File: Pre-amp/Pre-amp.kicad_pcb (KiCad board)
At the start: 2 copper layers, 182.9 x 53.3 mm, 137 parts, among them J1 In, J2 PWR, J3 Send, J4 Return, J5 Out, Q1 J113 NJFET, Q2 J113 NJFET, Q3 J113 NJFET, Q4 J113 NJFET, SW1 Jack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

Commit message: tweak PCB layout
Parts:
- C11, C12: value 0.01uf -> .01uf
- C13, C14: value 0.047uf -> .047uf
- C27: value 0.0047uf -> .0047uf
- C28: value 0.22uf -> .22uf
- C5: value 0.0033uf -> .0033uf
- C9: value 0.0022uf -> .0022uf
- D10: footprint LEDs:LED_D3.0mm -> Connector_PinHeader_2.00mm:PinHeader_2x01_P2.00mm_Vertical
- Q1, Q3: value J113 NJFET -> J113
- moved D10 20.0 mm to (125.5, 100.1), turned to 180 degrees
- moved R44 18.0 mm to (94.5, 64.3), turned to 90 degrees
- moved C19 13.2 mm to (130.1, 96.0), turned to 0 degrees
- moved R59 7.78 mm to (136.9, 98.0), turned to 0 degrees
- moved C17 7.34 mm to (89.2, 62.7)
- moved R46 5.66 mm to (98.6, 64.3), turned to 90 degrees
- moved R60 4.51 mm to (152.9, 83.8), turned to 0 degrees
- moved C29 4.15 mm to (145.1, 98.0)
- moved C33 4.02 mm to (109.0, 95.8)
- moved C18 3.82 mm to (127.0, 93.0), turned to 90 degrees
- moved R56 3.34 mm to (152.7, 79.2)
- moved C21 2.54 mm to (113.3, 73.7)
- moved C7 2.44 mm to (155.2, 60.5), turned to 180 degrees
- moved R61 2.30 mm to (157.7, 93.0)
- moved SW2 2.03 mm to (114.0, 100.1)
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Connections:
- J3 pad 3: (no net) -> Net-(J3-Pad3)
- J5 pad 3: (no net) -> Net-(J5-Pad3)
- SW1 pad 3: (no net) -> Net-(SW1-Pad3)
- SW2 pad 3: (no net) -> Net-(SW2-Pad3)
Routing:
- net F: track 80.1 -> 69.6 mm
- net D: track 55.6 -> 64.8 mm
- net B: track 11.8 -> 3.09 mm
- net DIST-IN: track 24.4 -> 32.8 mm
- net Net-(D10-Pad2): track 3.77 -> 7.39 mm
- net -15V: track 188.2 -> 184.7 mm
- net Net-(C26-Pad2): track 20.6 -> 17.3 mm
- net Net-(C21-Pad2): track 53.3 -> 51.0 mm
- net Net-(C6-Pad1): track 4.23 -> 6.49 mm
- net Net-(C8-Pad2): track 35.1 -> 36.8 mm
- net C: track 9.80 -> 11.4 mm
- net Net-(C8-Pad1): track 8.86 -> 10.4 mm
- net Net-(C20-Pad1): track 44.6 -> 46.0 mm
- net Net-(R13-Pad1): track 26.6 -> 27.6 mm
- net Net-(C33-Pad1): track 54.7 -> 55.7 mm
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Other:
- board text added: "MXM Designs Pre-Amp v1.2.0 05–11-2019"
- board text removed: "MXM Designs Pre-Amp v1.2.0 05–09-2019"

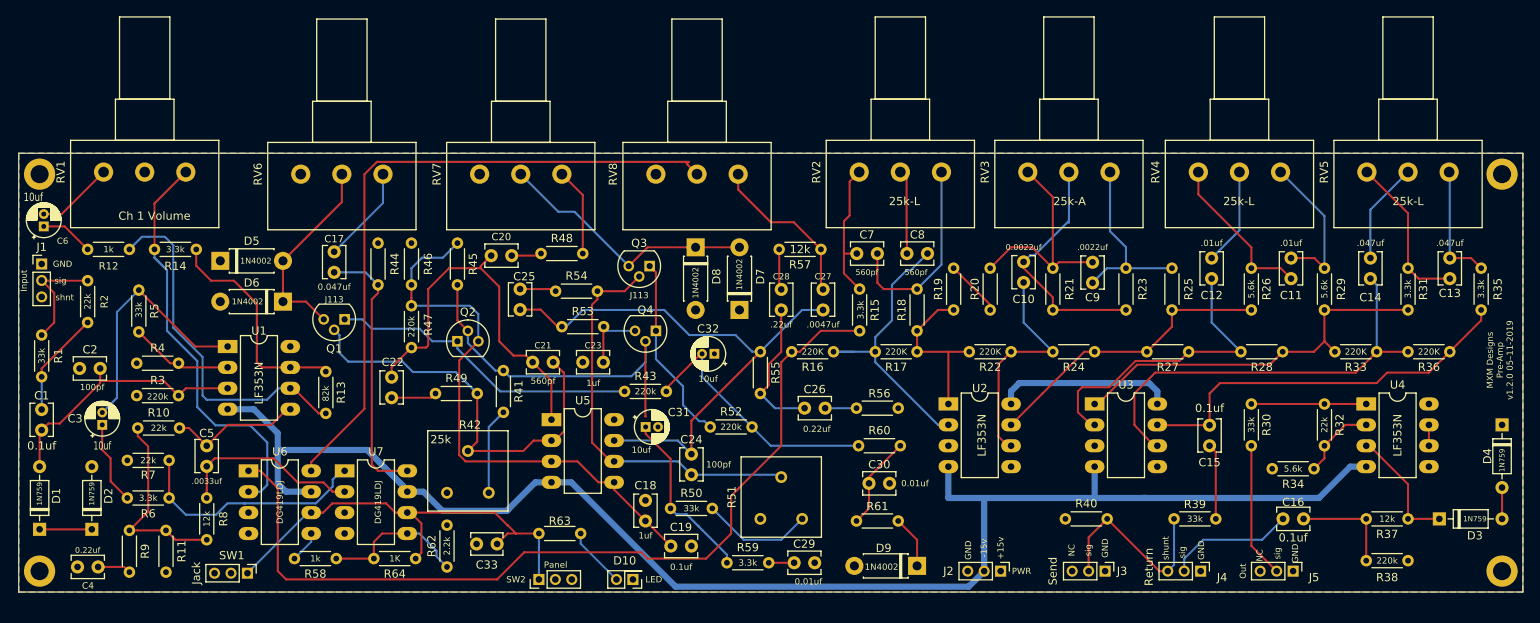
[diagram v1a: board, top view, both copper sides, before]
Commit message: add power caps
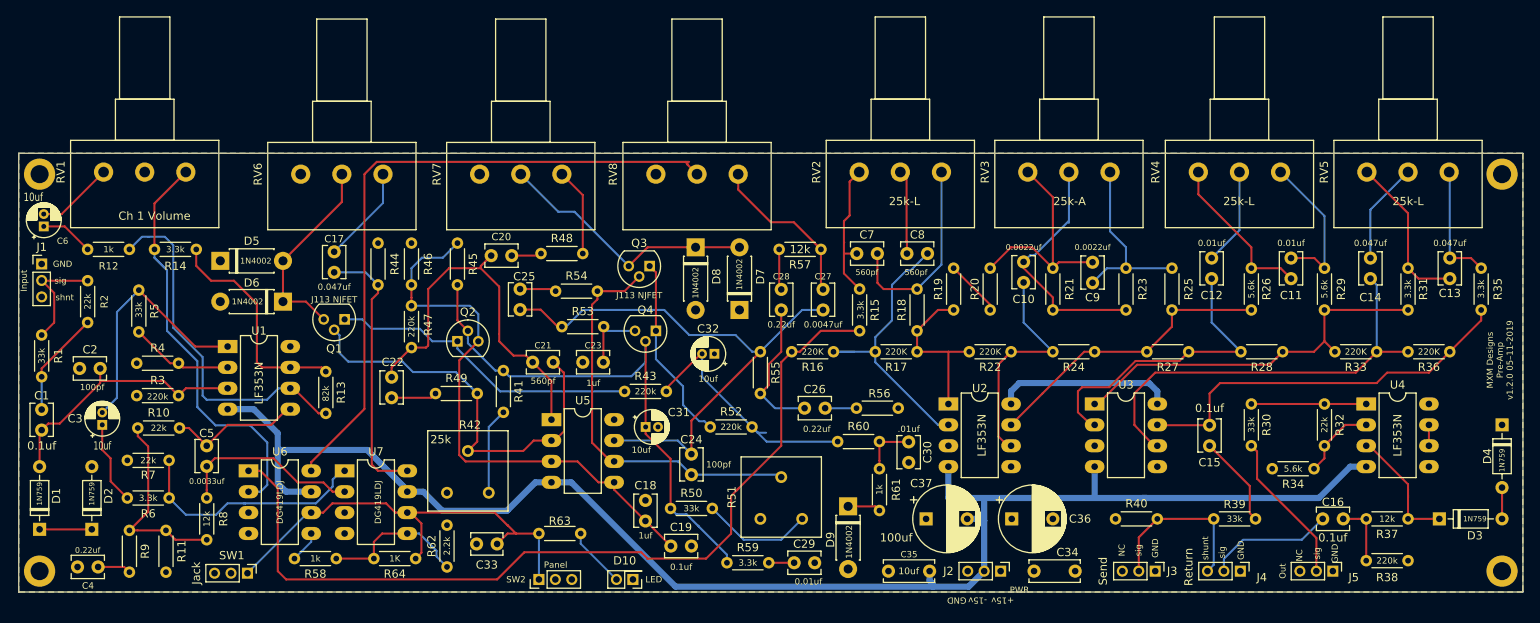
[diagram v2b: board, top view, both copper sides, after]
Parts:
- added C34: 10uf, Capacitor_THT:C_Disc_D6.0mm_W2.5mm_P5.00mm, F.Cu at (174.2, 99.1)
- added C35: 10uf, Capacitor_THT:C_Disc_D6.0mm_W2.5mm_P5.00mm, F.Cu at (156.5, 99.1)
- added C36: 100uf, Capacitor_THT:CP_Radial_D8.0mm_P5.00mm, F.Cu at (171.5, 92.7)
- added C37: 100uf, Capacitor_THT:CP_Radial_D8.0mm_P5.00mm, F.Cu at (161.1, 92.7)
- C11, C12: value .01uf -> 0.01uf
- C13, C14: value .047uf -> 0.047uf
- C27: value .0047uf -> 0.0047uf
- C28: value .22uf -> 0.22uf
- C30: value 0.01uf -> .01uf
- C5: value .0033uf -> 0.0033uf
- C9: value .0022uf -> 0.0022uf
- Q1, Q3: value J113 -> J113 NJFET
- moved D9 11.1 mm to (151.6, 91.2), turned to 270 degrees
- moved J3 6.10 mm to (189.0, 99.1)
- moved R40 6.10 mm to (184.2, 92.7)
- moved C16 4.83 mm to (209.3, 92.7)
- moved J4 4.83 mm to (199.3, 99.1)
- moved J5 4.83 mm to (210.6, 99.1)
- moved R39 4.83 mm to (196.1, 92.7)
- moved C30 3.44 mm to (159.0, 85.9), turned to 90 degrees
- moved R61 2.62 mm to (155.4, 91.7), turned to 90 degrees
- moved R60 2.59 mm to (150.4, 83.3)
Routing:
- net Net-(C16-Pad2): track 12.7 -> 7.87 mm
- net C: track 11.4 -> 6.87 mm
- net -15V: track 184.7 -> 188.9 mm
- net Net-(J3-Pad2): track 23.9 -> 20.8 mm
- net Net-(C15-Pad1): track 9.21 -> 12.3 mm
- net Net-(D9-Pad1): track 6.41 -> 4.02 mm
- net Net-(J5-Pad2): track 16.5 -> 18.5 mm
- net D: track 64.8 -> 66.0 mm
- net E: track 31.4 -> 30.6 mm

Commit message: Rearrange the board for taller things to be away from the edges.
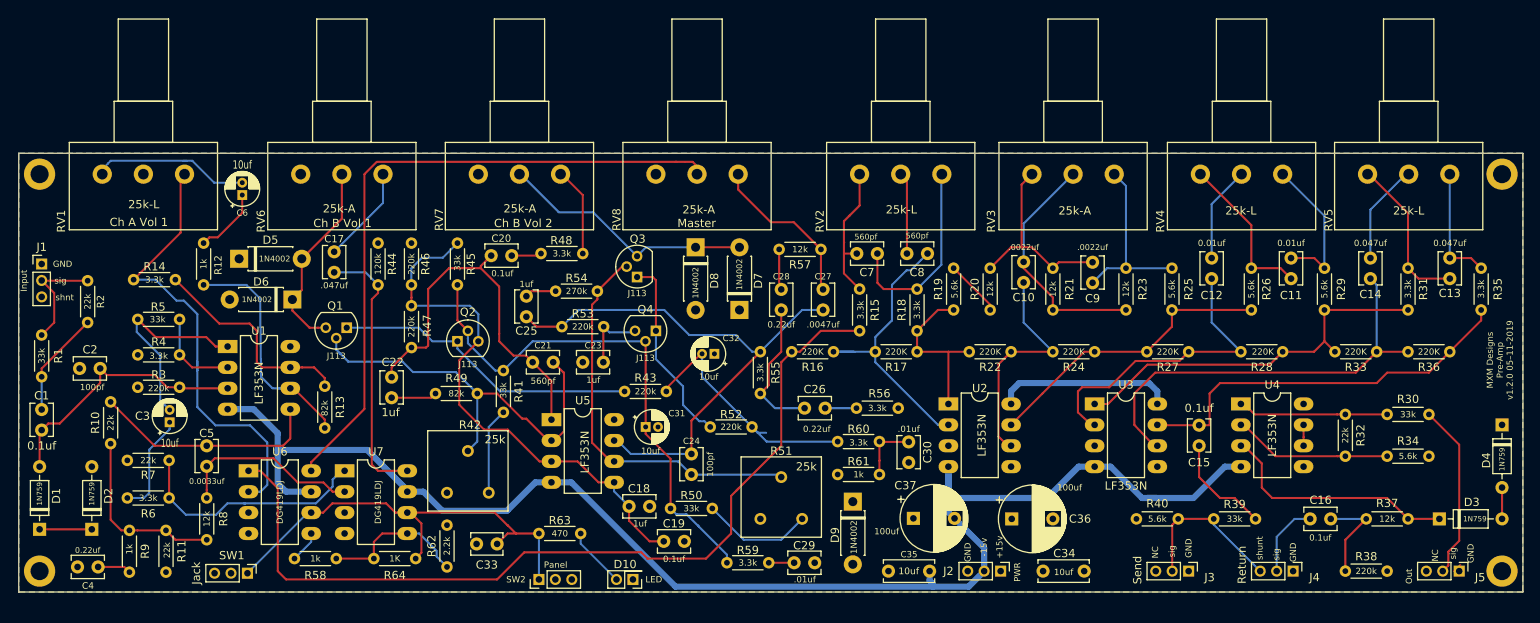
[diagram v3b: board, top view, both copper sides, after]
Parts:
- C10, C9: value 0.0022uf -> .0022uf
- C17: value 0.047uf -> .047uf
- C27: value 0.0047uf -> .0047uf
- C29: value 0.01uf -> .01uf
- Q1, Q2, Q3, Q4: value J113 NJFET -> J113
- moved C6 24.4 mm to (78.0, 53.3)
- moved R30 16.6 mm to (217.2, 80.0), turned to 0 degrees
- moved J5 15.4 mm to (225.9, 99.1)
- moved U4 15.2 mm to (199.4, 78.7)
- moved R12 14.1 mm to (73.3, 59.2), turned to 270 degrees
- moved R34 9.02 mm to (217.2, 85.1), turned to 0 degrees
- moved C3 8.20 mm to (69.2, 81.0)
- moved R61 6.71 mm to (150.4, 87.3), turned to 0 degrees
- moved J4 6.41 mm to (205.7, 99.1)
- moved R5 5.18 mm to (70.4, 68.5), turned to 180 degrees
- moved R14 4.47 mm to (64.8, 63.6)
- moved J3 4.06 mm to (193.0, 99.1)
- moved R10 3.81 mm to (62.0, 83.6), turned to 90 degrees
- moved R32 2.84 mm to (212.1, 80.0)
- moved R38 2.84 mm to (212.1, 99.1)
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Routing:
- net Net-(D3-Pad1): track 15.3 -> 29.5 mm
- net Net-(R12-Pad2): track 43.6 -> 29.5 mm
- net -15V: track 188.9 -> 177.1 mm
- net Net-(C5-Pad2): track 16.2 -> 28.0 mm
- net Net-(C6-Pad2): track 9.39 -> 19.6 mm
- net Net-(R32-Pad2): track 9.45 -> 19.4 mm
- net Net-(C16-Pad1): track 15.5 -> 9.14 mm
- net Net-(C3-Pad2): track 30.4 -> 25.0 mm
- net Net-(R30-Pad1): track 14.0 -> 18.3 mm
- net Net-(D9-Pad1): track 4.02 -> 0.00 mm
- net Net-(C16-Pad2): track 7.87 -> 11.7 mm
- net F: track 69.6 -> 65.8 mm
- net Net-(C9-Pad2): track 27.8 -> 24.3 mm
- net CLEAN-OUT: track 52.2 -> 55.3 mm
- net Net-(J5-Pad2): track 18.5 -> 21.4 mm
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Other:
- board text added: "Ch A Vol 1"
- board text added: "Ch B Vol 1"
- board text added: "Ch B Vol 2"
- board text added: "Master"
- board text removed: "Ch 1 Volume"

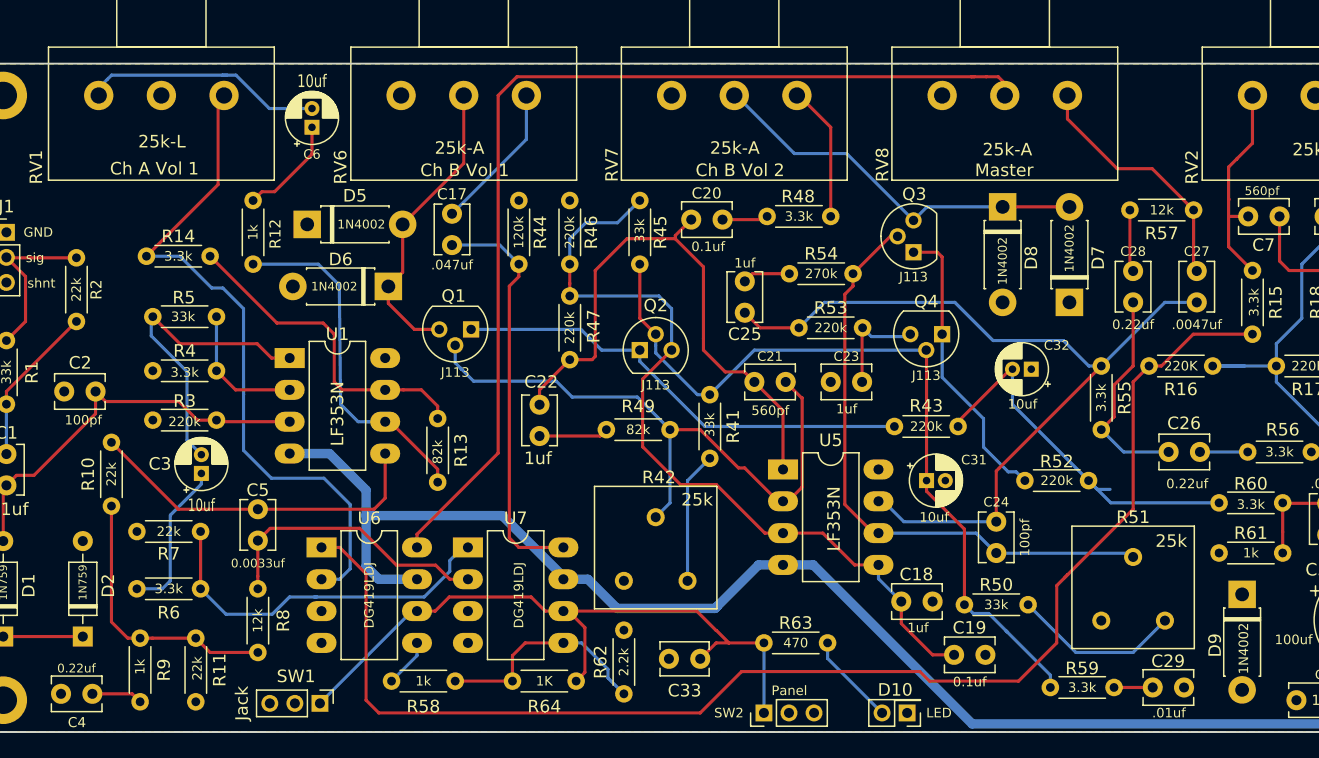
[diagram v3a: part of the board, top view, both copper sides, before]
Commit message: Add IOBoard
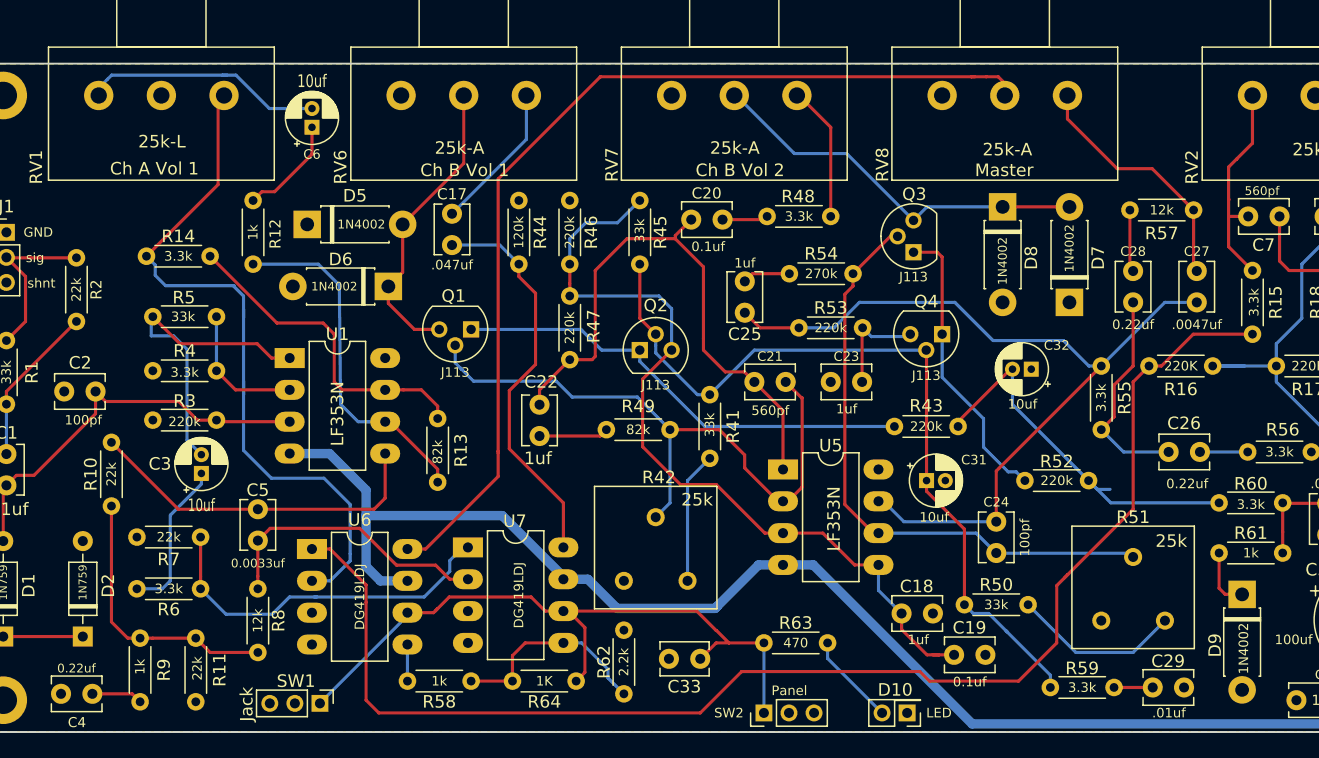
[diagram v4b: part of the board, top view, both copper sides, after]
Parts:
- moved R58 1.27 mm to (90.7, 97.5)
- moved C18 0.95 mm to (125.0, 92.1)
- moved U6 0.77 mm to (78.0, 87.0)
- moved R7 0.44 mm to (64.0, 86.0)
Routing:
- net Net-(D9-Pad1): track 0.00 -> 4.86 mm
- net DIST-OUT: track 81.2 -> 78.8 mm
- net CLEAN-OUT: track 55.3 -> 57.6 mm
- net Net-(R58-Pad1): track 18.0 -> 16.7 mm
- net Net-(C33-Pad1): track 55.7 -> 56.8 mm
- net Net-(C3-Pad2): track 25.0 -> 26.0 mm
- net DIST-IN: track 32.8 -> 31.8 mm
- net Net-(R58-Pad2): track 3.89 -> 2.92 mm
- net F: track 65.8 -> 66.6 mm
- net -15V: track 177.1 -> 176.4 mm
- net Net-(C21-Pad2): track 50.7 -> 51.3 mm

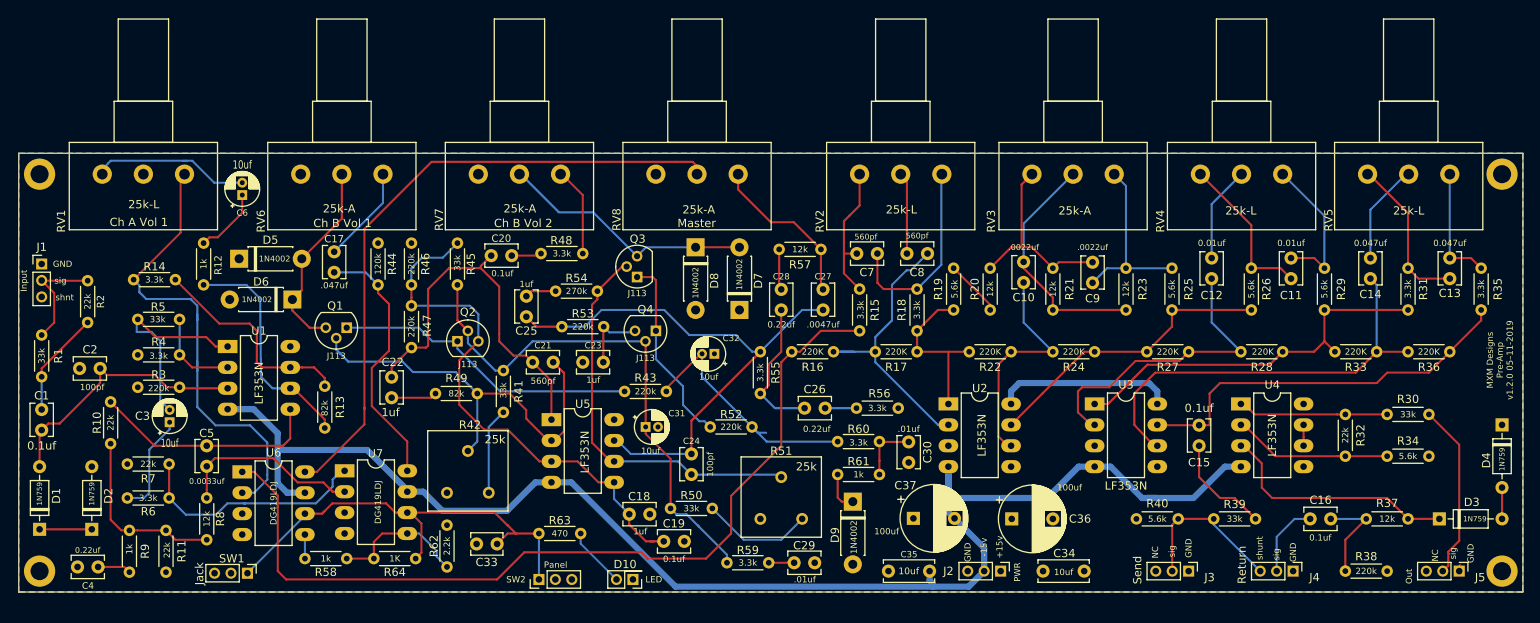
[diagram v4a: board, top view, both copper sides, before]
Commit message: fix 1uf caps to CP
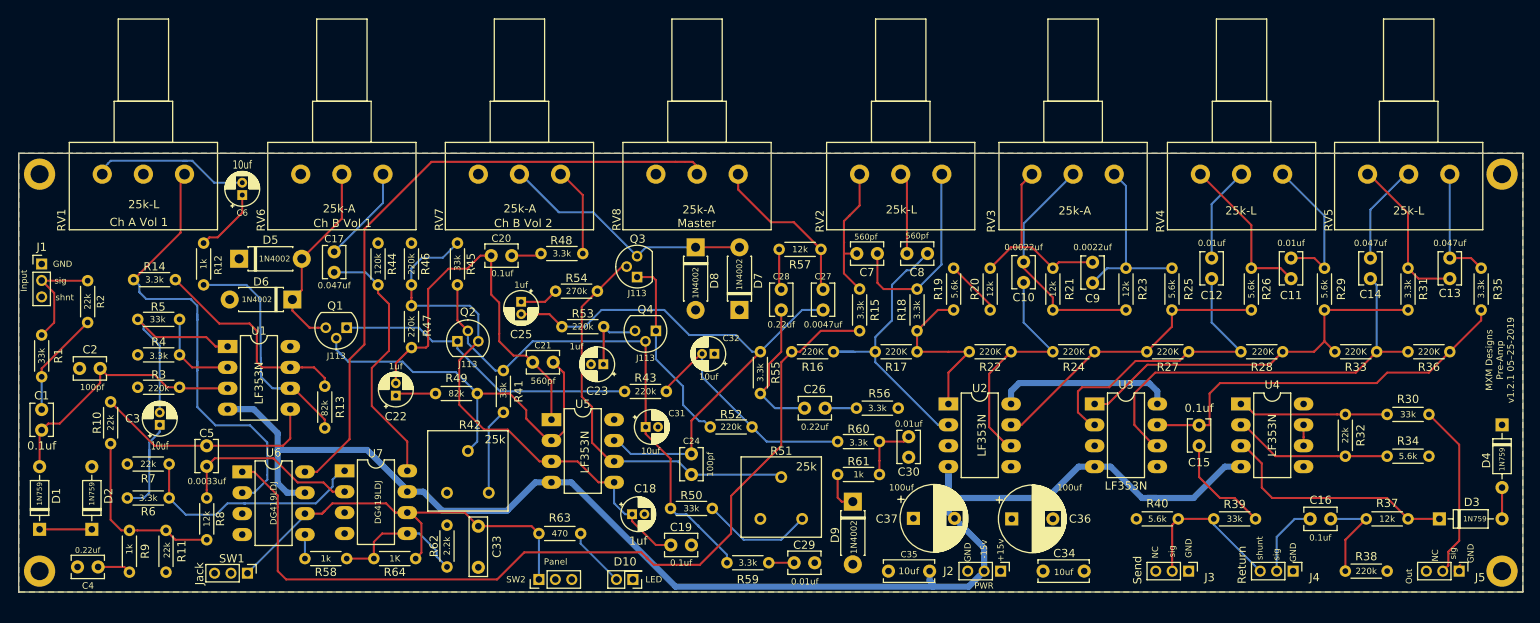
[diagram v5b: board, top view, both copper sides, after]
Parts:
- C10, C9: value .0022uf -> 0.0022uf
- C17: value .047uf -> 0.047uf
- C18, C22, C23, C25: footprint Capacitor_THT:C_Disc_D3.8mm_W2.6mm_P2.50mm -> Capacitor_THT:CP_Radial_D4.0mm_P1.50mm
- C27: value .0047uf -> 0.0047uf
- C29, C30: value .01uf -> 0.01uf
- C33: footprint Capacitors_THT:C_Disc_D3.8mm_W2.6mm_P2.50mm -> Capacitor_THT:C_Rect_L7.0mm_W2.0mm_P5.00mm
- moved C33 3.14 mm to (106.7, 93.6), turned to 270 degrees
- moved C3 1.25 mm to (67.9, 81.3)
- moved C19 0.97 mm to (130.1, 95.9)
- moved C25 0.93 mm to (111.9, 66.3)
- moved C30 0.64 mm to (159.0, 85.2)
- moved C22 0.57 mm to (96.6, 77.7)
- moved C18 0.34 mm to (125.4, 92.1)
- moved C23 0.25 mm to (121.9, 73.9)
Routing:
- net Net-(C33-Pad1): track 56.8 -> 54.0 mm
- net Net-(C20-Pad1): track 46.0 -> 47.3 mm
- net Net-(C3-Pad2): track 26.0 -> 24.7 mm
- net Net-(R17-Pad1): track 20.7 -> 21.8 mm
- net Net-(C24-Pad2): track 48.2 -> 49.3 mm
- net E: track 30.6 -> 29.6 mm
- net Net-(C10-Pad2): track 27.9 -> 28.8 mm
- net Net-(C25-Pad1): track 3.81 -> 4.73 mm
- net TONE-IN: track 108.0 -> 108.8 mm
- net Net-(C24-Pad1): track 67.6 -> 68.4 mm
- net Net-(C22-Pad1): track 5.54 -> 4.93 mm
- net F: track 66.6 -> 67.1 mm
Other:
- board text added: "MXM Designs Pre-Amp v1.2.1 05–25-2019"
- board text removed: "MXM Designs Pre-Amp v1.2.0 05–11-2019"
